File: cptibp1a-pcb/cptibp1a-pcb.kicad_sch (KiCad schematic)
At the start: 24 parts, among them J1 10118194-0001LF, J2 PAD+, J3 PAD-, Q1 2N7002, Q2 AO3413, U1 NCP360SNT, U2 APX809S-31SA, U3 BQ21040, U4 APX810S-44SA, U5 NCP380HSN05

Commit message: rev1
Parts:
- added C3: 4u7, Capacitor_SMD:C_0805_2012Metric, symbol Device:C
- added R6: 10k, Resistor_SMD:R_0805_2012Metric, symbol Device:R
- added U5: MAX40203AUK, george:SOT-23-5_TI_DBV5, symbol Analog_Switch:MAX40200AUK
- renumbered U5 to U6
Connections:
- net B+: now also U5.1 (VDD); no longer U6.5 (IN)
- net EN: now also U5.3 (EN); no longer U6.4 (EN)
- net GND: now also C3.2, R6.1, U5.2 (GND)
- net VOUT: now also U6.4 (EN), U6.5 (IN), C3.1, U5.5 (OUT); no longer C6.1, C7.1, D3.1 (K), J2.1 (Pin_1), U4.3 (VCC), U6.1 (OUT)
- net at U6.3 (~{OC}): now also R6.2
- new net VOUTF: C6.1, C7.1, D3.1 (K), J2.1 (Pin_1), U4.3 (VCC), U6.1 (OUT)
- no-connect marks 5 -> 4
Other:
- note added: "CHANGE HISTORY: REV1: C2 --> 0u1 Add U6, R6 F1 --> remove"
- note removed: "CHANGE HISTORY: REV1: C2 --> 0u1 U5 --> NCP380HSN05 F1 --> remove"
- moved on the sheet: U6

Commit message: Rev1 update (minor)
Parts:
- added D4: DBRIDGE, symbol Device:D_Bridge_+-AA
- added J4: PAD-, symbol Connector:Conn_01x01_Pin
- added J5: PAD+, symbol Connector:Conn_01x01_Pin
- added J6: ACIN, symbol Connector_Generic:Conn_01x02
- added R7: 47, symbol Device:R
- added SW1: POWER, symbol Switch:SW_DPST
- R5: now not fitted
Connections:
- new net: D4.2 (-), R7.2, SW1.3
- new net: D4.3, J6.1 (Pin_1)
- new net: D4.4, J6.2 (Pin_2)
- new net CALC_VBAT-: J4.1 (Pin_1), R7.1, SW1.1, SW1.2, SW1.4
- new net CALC_VSS: D4.1 (+), J5.1 (Pin_1)
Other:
- note added: "--> 3.1~4.2V 200mA (ON), limited 800mA <-- <5.6V (zener)"
- note added: "3.1~4.2V (battery)"
- note added: "4.35~4.85V (USB) 4.40~5.60V (calc)"
- note added: "4.75~5.25V"
- note added: "5VAC"
- note added: "CALCULATOR"
- note added: "CHANGE HISTORY: REV1: C2 --> 0u1 Add U6, R6, C3 F1 --> remove U4/pin3 --> VOUTF Add calculator schematic"
- note added: "Low battery indicator at 3.30V"
- note added: "off at 3.1V"
- note removed: "--> 200mA (ON) <-- 5VAC rectified via 47ohm (7Vpk)"
- note removed: "CALC: <6V"
- note removed: "CHANGE HISTORY: REV1: C2 --> 0u1 Add U6, R6 F1 --> remove"
- note removed: "Low battery at 3.30V"
- note removed: "off at 3V"
- moved on the sheet: BT1, C4, U2

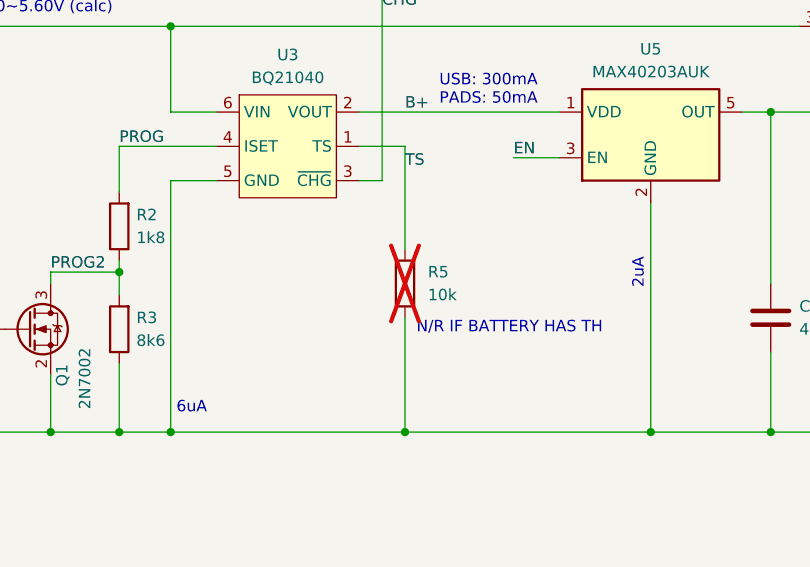
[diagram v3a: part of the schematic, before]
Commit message: remove nonpop
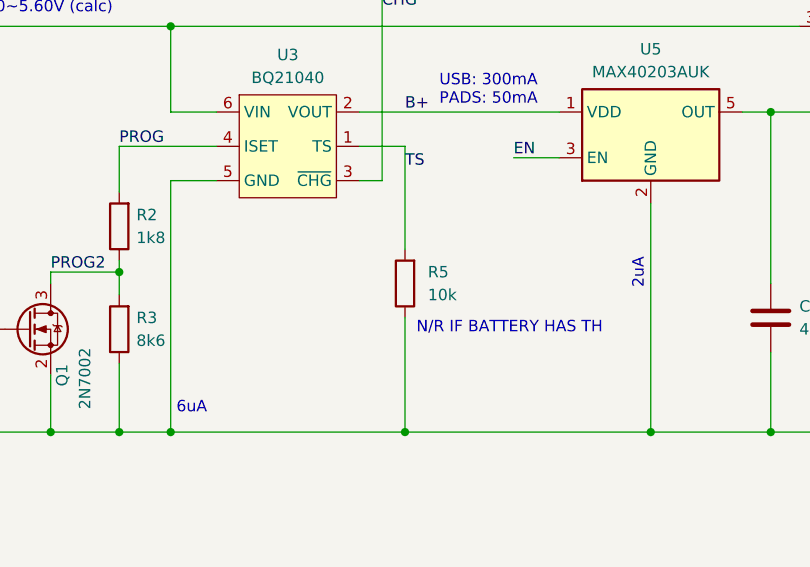
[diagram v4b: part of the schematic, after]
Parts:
- R5: now fitted
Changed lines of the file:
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@@
   )
   (symbol (lib_id "Device:R") (at 145.415 86.995 180) (unit 1)
-    (in_bom yes) (on_board yes) (dnp yes) (fields_autoplaced)
+    (in_bom yes) (on_board yes) (dnp no) (fields_autoplaced)
     (property "Reference" "R5" (at 147.955 85.725 0)
       (effects (font (size 1.27 1.27)) (justify right))
